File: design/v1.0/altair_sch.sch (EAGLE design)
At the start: 68 parts, among them J1 TYPE-C-31-M-12, J2 USB-A-S-X-X-TH, J3 22-03-5035, J4 22-03-5035, J5 22-03-5035, J6 22-03-5035, J7 22-03-5035, Q1 IRF9540, Q10 NPN, Q2 IRF9540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

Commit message: File type changed (9.x compatible)
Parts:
- added S1, S2: MOMENTARY-SWITCH-SPST-SMD-6.2MM-TALL, SparkFun-Switches:MOMENTARY-SWITCH-SPST-SMD-6.2MM-TALL
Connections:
- net ESP_EN: now also S1.1
- net ESP_IO0: now also S2.1
- net GND: now also S1.2, S2.2

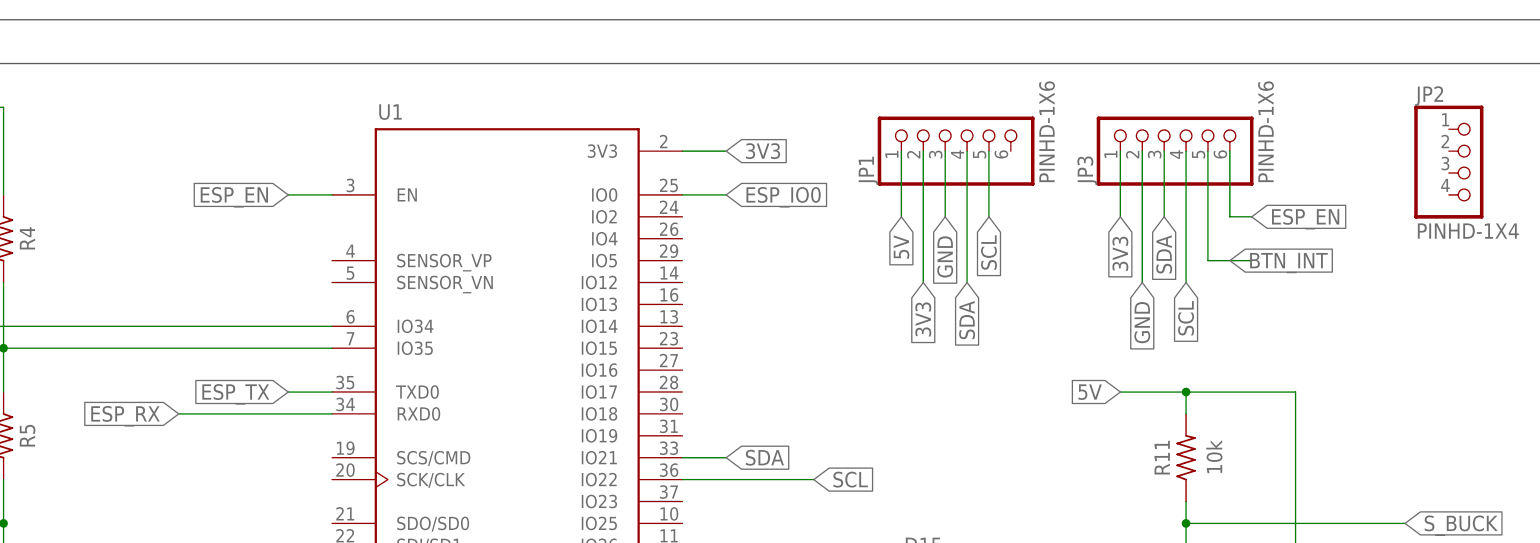
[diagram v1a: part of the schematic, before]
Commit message: Button interrupt added
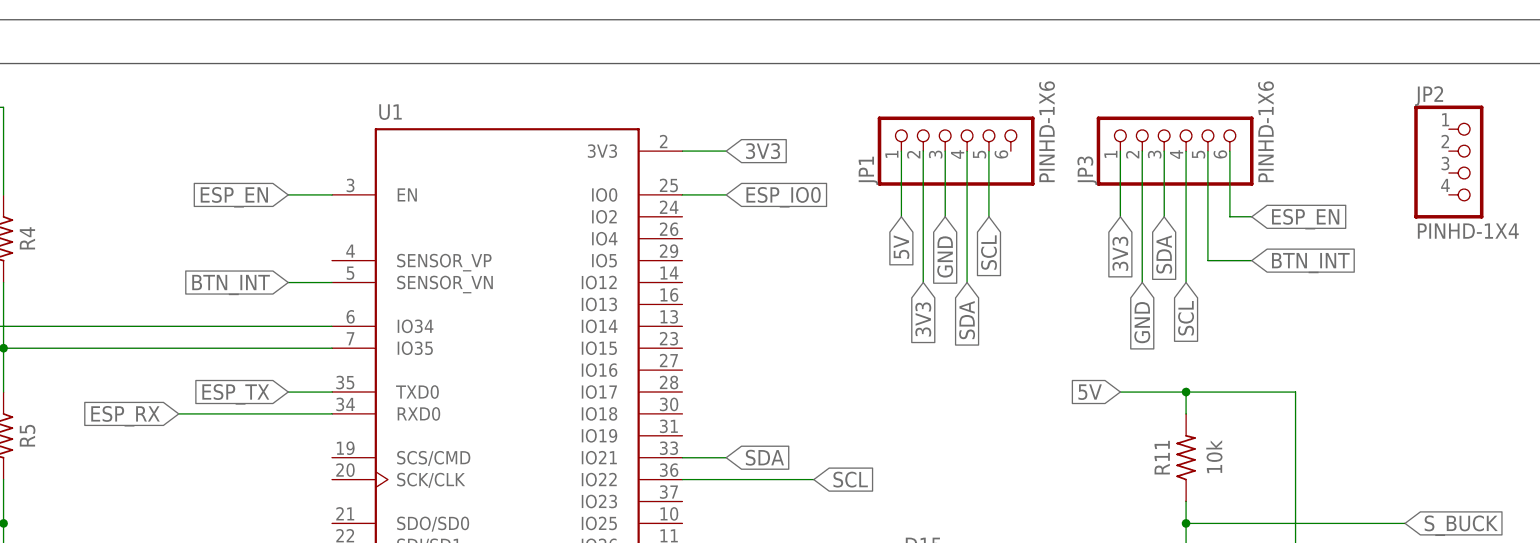
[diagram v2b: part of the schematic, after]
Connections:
- net BTN_INT: now also U1.SENSOR_VN
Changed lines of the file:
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@@
 <wire x1="-17.78" y1="-91.44" x2="-17.78" y2="-104.14" width="0.1524" layer="91"/>
 <wire x1="-17.78" y1="-104.14" x2="-12.7" y2="-104.14" width="0.1524" layer="91"/>
-<label x="-15.24" y="-104.14" size="1.778" layer="95" xref="yes"/>
+<label x="-12.7" y="-104.14" size="1.778" layer="95" xref="yes"/>
 <pinref part="JP3" gate="A" pin="5"/>
 </segment>
+<segment>
+<pinref part="U1" gate="G$1" pin="SENSOR_VN"/>
+<wire x1="-119.38" y1="-106.68" x2="-124.46" y2="-106.68" width="0.1524" layer="91"/>
+<label x="-124.46" y="-106.68" size="1.778" layer="95" rot="R180" xref="yes"/>
+</segment>
 </net>
